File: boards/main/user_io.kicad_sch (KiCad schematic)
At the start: 21 parts, among them J6 FH12-6S-0.5SH(55), J7 FH12-10S-0.5SH(55), P1 JST_BTN_1, P2 JST_BTN_2, P3 JST_BTN_3, U6 BNO085, U7 DRV2605LDGSR

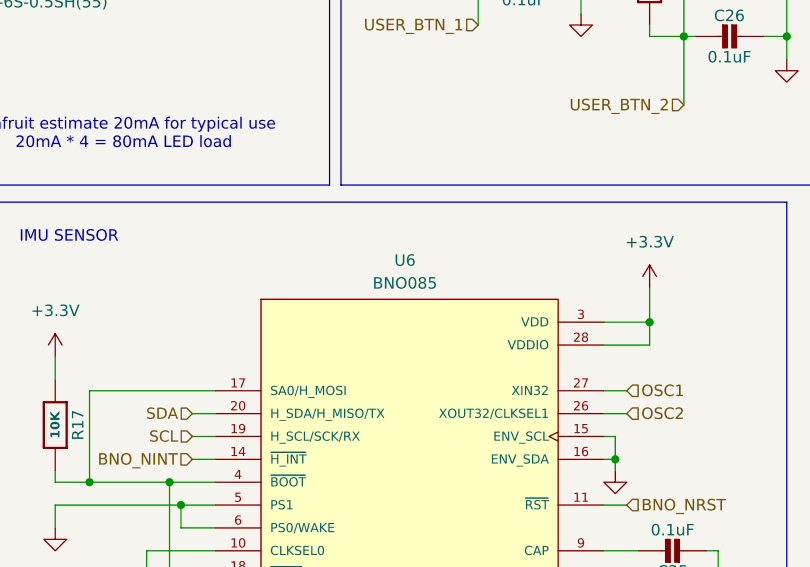
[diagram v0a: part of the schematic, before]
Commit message: Board migrations. Move to newer LED and IMU
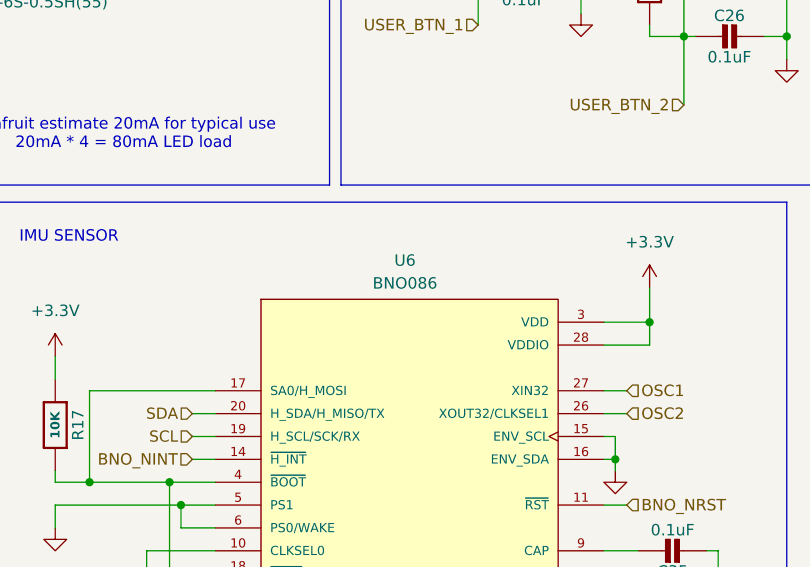
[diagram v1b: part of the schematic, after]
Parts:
- C23, C24, C26, C35: Dielectric (none) -> X7R; DigiKey_PN (none) -> 1276-6844-1-ND; MPN 0402B104K160HI -> CL05B104KO5VPNC; Manufacturer (none) -> Samsung Electro-Mechanics; Voltage (none) -> 16V
- C46, C47: Dielectric (none) -> X7R; DigiKey_PN (none) -> 1276-1184-1-ND; MPN 0603B105K100XD -> CL10B105KA8NNNC; Manufacturer (none) -> Samsung Electro-Mechanics; Voltage (none) -> 25V
- D2: DigiKey_PN (none) -> BAV199LT1GOSCT-ND; MPN BAV199 -> BAV199LT1G; Manufacturer (none) -> onsemi; Sourcing_Note (none) -> OVERSTRESSED AS DRAWN. Pin 3 is the common K1/A2 node, so o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
- HAPTIC1, P1, P2, P3: DigiKey_PN (none) -> 455-1564-1-ND; Manufacturer (none) -> JST Sales America Inc.
- J6: DigiKey_PN (none) -> HFJ106CT-ND; MPN (none) -> FH12-6S-0.5SH(55); Manufacturer (none) -> Hirose Electric Co Ltd; Sourcing_Note (none) -> Digi-Key stock 0, 16-week factory lead. Alternatives: stand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
- J7: DigiKey_PN (none) -> HFJ110CT-ND; MPN (none) -> FH12-10S-0.5SH(55); Manufacturer (none) -> Hirose Electric Co Ltd
- R13: DigiKey_PN (none) -> 13-RT0603BRC07500RLCT-ND; Manufacturer (none) -> YAGEO; Sourcing_Note (none) -> 500R is not an E24 value, so this is a 0.1% thin-film part 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; Tolerance (none) -> 0.1%
- R14, R15, R16, R17: DigiKey_PN (none) -> 311-10.0KHRCT-ND; Manufacturer (none) -> YAGEO; Tolerance (none) -> 1%
- U6: value BNO085 -> BNO086; symbol BNO085:BNO085 -> BNO086:BNO086; DigiKey_PN (none) -> 1888-BNO086CT-ND; MANUFACTURER Hillcrest Laboratories, Inc. -> CEVA Technologies, Inc.; MP BNO085 -> BNO086; MPN BNO085 -> BNO086; Manufacturer (none) -> CEVA Technologies, Inc.; PRICE 10.06 -> 11.62; Sourcing_Note (none) -> BNO086 replaces the deprecated BNO085. Same 28-LGA 5.2x3.8x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
- U7: DigiKey_PN (none) -> 296-40032-1-ND; Manufacturer (none) -> Texas Instruments; Sourcing_Note (none) -> Only ~105 pieces in Digi-Key stock with a 16-week factory l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

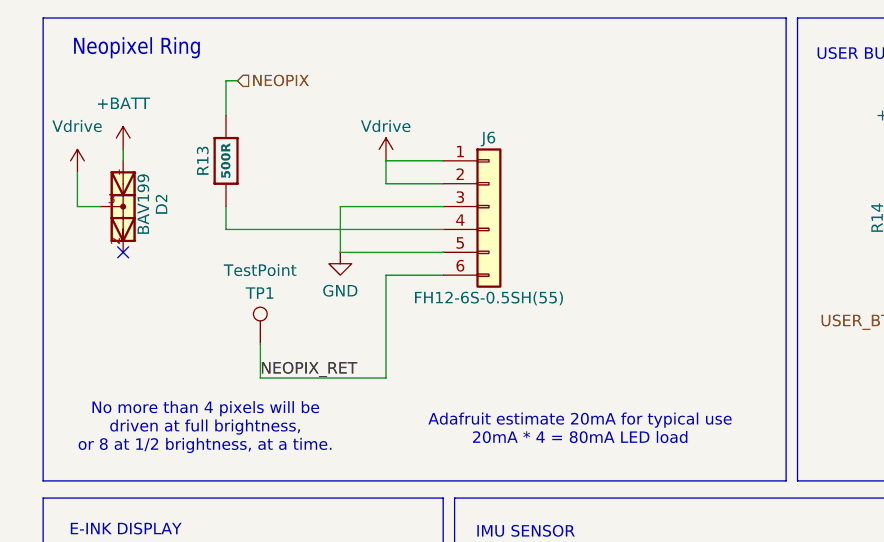
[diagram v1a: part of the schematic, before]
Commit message: some more component reworking. Moved to 10 lane ribbon connects between all boards
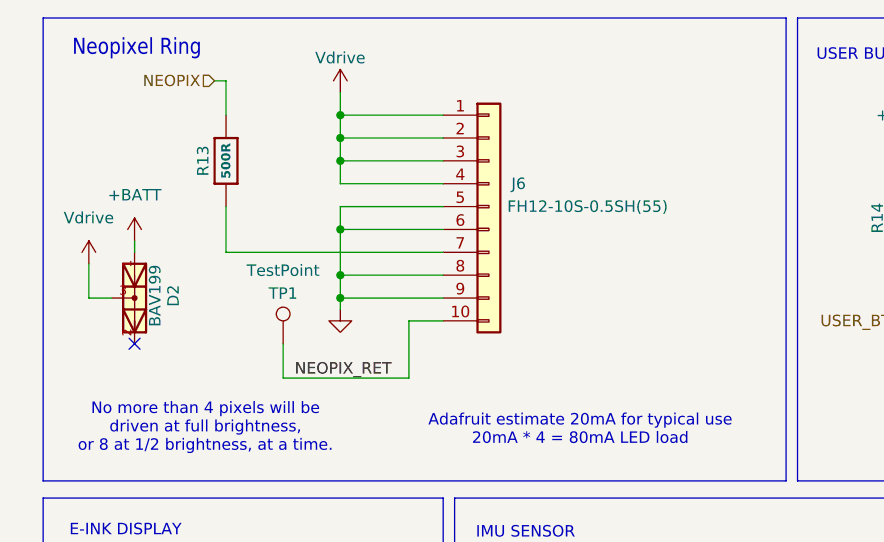
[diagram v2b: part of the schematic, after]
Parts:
- removed J6: FH12-6S-0.5SH(55), Connector_FFC-FPC:Hirose_FH12-6S-0.5SH_1x06-1MP_P0.50mm_Horizontal, symbol Connector_Generic:Conn_01x06
- added J6: FH12-10S-0.5SH(55), Connector_FFC-FPC:Hirose_FH12-10S-0.5SH_1x10-1MP_P0.50mm_Horizontal, symbol Connector_Generic:Conn_01x10
- C23, C24, C26, C35, C46, C47: symbol Adafruit ESP32-S3 8MB No PSRAM-eagle-import:CAP_CERAMIC0603_NO -> smart_compass_main:CAP_CERAMIC0603_NO
- D2: symbol BAV199:BAV199 -> smart_compass_main:BAV199
- HAPTIC1, P1, P2, P3: symbol SM02B-GHS-TB:SM02B-GHS-TB -> smart_compass_main:SM02B-GHS-TB
- R13, R14, R15, R16, R17: symbol Adafruit ESP32-S3 8MB No PSRAM-eagle-import:RESISTOR_0603_NOOUT -> smart_compass_main:RESISTOR_0603_NOOUT
- U6: symbol BNO086:BNO086 -> smart_compass_main:BNO086
- U7: symbol DRV2605LDGSR:DRV2605LDGSR -> smart_compass_main:DRV2605LDGSR
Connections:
- net GND: now also J6.5 (Pin_5), J6.6 (Pin_6), J6.8 (Pin_8), J6.9 (Pin_9)
- net NEOPIX_RET: now also J6.10 (Pin_10)
- net Vdrive: now also J6.1 (Pin_1), J6.2 (Pin_2), J6.3 (Pin_3), J6.4 (Pin_4)
- net at R13.1: now also J6.7 (Pin_7)
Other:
- moved on the sheet: D2, TP1

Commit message: Add a voltage booster and logic shift to the LED ring. Power consumption implications, but necessary
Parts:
- removed D2: BAV199, BAV199:SOT23, symbol smart_compass_main:BAV199
- added C15: 22uF, Capacitor_SMD:C_0805_2012Metric, symbol Device:C
- added FB1: 600R@100MHz, Inductor_SMD:L_0603_1608Metric, symbol Device:FerriteBead
- HAPTIC1, P1, P2, P3: footprint SM02B-GHS-TB:JST_SM02B-GHS-TB -> (none)
- J3: renamed from J6; Sourcing_Note Standardised on the 10-way FH12 shared with the display lin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 -> Vdrive on 1-3, RING_EN on 4, GND on 5, 6, 8, 9, NEOPIX on 7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
- R13: Sourcing_Note 500R is not an E24 value, so this is a 0.1% thin-film part at $0.25. For a series damping resistor a 5% 510R (RC0603JR-07511RL) would do the same job for about $0.01. -> 500R is not an E24 value, so this is a 0.1% thin-film part at $0.25. For a series damping resistor a 5% 510R (RC0603JR-07511RL) would do the same job for about $0.01. It has a second job now the ring runs at 5V: when RING_EN is low the ring board's level shifter is unpowered, and this resistor limits the current into its input clamp if firmware drives NEOPIX high while the ring is off.
- U6: footprint BNO085:IC_BNO085 -> (none)
- U7: footprint DRV2605LDGSR:SOP50P490X110-10N -> (none)
- renumbered C23 to C16, C24 to C17, C26 to C18, C35 to C19, C46 to C20, C47 to C21, J7 to J4
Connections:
- net +BATT: now also FB1.1
- net GND: now also C15.2
- net Vdrive: now also C15.1, FB1.2; no longer J3.4 (Pin_4)
- new net RING_EN: J3.4 (Pin_4)
- no-connect marks 1 -> 0
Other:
- note removed: "No more than 4 pixels will be driven at full brightness, or 8 at 1/2 brightness, at a time."

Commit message: Update the footprint for the flash chip
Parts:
- renumbered C15 to C14, C16 to C15, C17 to C16, C18 to C17, C19 to C18, C20 to C19, C21 to C20

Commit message: UPGRADE 1UF CAPACITORS
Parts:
- C19, C20: DigiKey_PN 1276-1184-1-ND -> 445-C1608X7R1H105K080ABCT-ND; MPN CL10B105KA8NNNC -> C1608X7R1H105K080AB; Manufacturer Samsung Electro-Mechanics -> TDK; PRICE 0.05765 -> 0.0615; Tolerance (none) -> 10%; Voltage 25V -> 50V
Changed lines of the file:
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@@
 			)
 		)
-		(property "Datasheet" ""
+		(property "Datasheet" "https://product.tdk.com/system/files/dam/doc/product/capacitor/ceramic/mlcc/catalog/mlcc_commercial_general_en.pdf"
 			(at 83.82 163.83 0)
 			(hide yes)
@@
 			)
 		)
-		(property "MPN" "CL10B105KA8NNNC"
+		(property "MPN" "C1608X7R1H105K080AB"
 			(at 83.82 163.83 90)
 			(hide yes)
@@
 			)
 		)
-		(property "PRICE" "0.05765"
+		(property "PRICE" "0.0615"
 			(at 83.82 163.83 90)
 			(hide yes)
@@
 			)
 		)
-		(property "Manufacturer" "Samsung Electro-Mechanics"
+		(property "Manufacturer" "TDK"
 			(at 83.82 163.83 0)
 			(hide yes)
@@
 			)
 		)
-		(property "DigiKey_PN" "1276-1184-1-ND"
+		(property "DigiKey_PN" "445-C1608X7R1H105K080ABCT-ND"
 			(at 83.82 163.83 0)
 			(hide yes)
@@
 			)
 		)
-		(property "Voltage" "25V"
+		(property "Voltage" "50V"
 			(at 83.82 163.83 0)
 			(hide yes)
@@
 			)
 		)
+    (property "Tolerance" "10%" (at 83.82 163.83 0)
+      (effects (font (size 1.27 1.27)) (hide yes))
+    )
 		(pin "1"
 		)
@@
 			)
 		)
-		(property "Datasheet" ""
+		(property "Datasheet" "https://product.tdk.com/system/files/dam/doc/product/capacitor/ceramic/mlcc/catalog/mlcc_commercial_general_en.pdf"
 			(at 20.32 148.59 0)
 			(hide yes)
@@
 			)
 		)
-		(property "MPN" "CL10B105KA8NNNC"
+		(property "MPN" "C1608X7R1H105K080AB"
 			(at 20.32 148.59 90)
 			(hide yes)
@@
 			)
 		)
-		(property "PRICE" "0.05765"
+		(property "PRICE" "0.0615"
 			(at 20.32 148.59 90)
 			(hide yes)
@@
 			)
 		)
-		(property "Manufacturer" "Samsung Electro-Mechanics"
+		(property "Manufacturer" "TDK"
 			(at 20.32 148.59 0)
 			(hide yes)
@@
 			)
 		)
-		(property "DigiKey_PN" "1276-1184-1-ND"
+		(property "DigiKey_PN" "445-C1608X7R1H105K080ABCT-ND"
 			(at 20.32 148.59 0)
 			(hide yes)
@@
 			)
 		)
-		(property "Voltage" "25V"
+		(property "Voltage" "50V"
 			(at 20.32 148.59 0)
 			(hide yes)
@@
 			)
 		)
+    (property "Tolerance" "10%" (at 20.32 148.59 0)
+      (effects (font (size 1.27 1.27)) (hide yes))
+    )
 		(pin "1"
 		)

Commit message: Ditch the JST for the buttons, power switch, and haptic motor. Just solder direct
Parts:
- removed HAPTIC1: JST_HAPTIC, symbol smart_compass_main:SM02B-GHS-TB
- removed P1: JST_BTN_1, symbol smart_compass_main:SM02B-GHS-TB
- removed P2: JST_BTN_2, symbol smart_compass_main:SM02B-GHS-TB
- removed P3: JST_BTN_3, symbol smart_compass_main:SM02B-GHS-TB
- added HAPTIC1: HAPTIC_PADS, Connector_Wire:SolderWire-0.127sqmm_1x02_P3.7mm_D0.48mm_OD1mm_Relief, symbol Connector_Generic:Conn_01x02
- added P1: BUTTON_PADS, Connector_Wire:SolderWire-0.127sqmm_1x04_P3.7mm_D0.48mm_OD1mm_Relief, symbol Connector_Generic:Conn_01x04
- renumbered C16 to C15, C17 to C16, C15 to C17, R15 to R14, R16 to R15, R14 to R16
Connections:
- net GND: now also P1.4 (Pin_4)
- net USER_BTN_1: now also P1.1 (Pin_1)
- net USER_BTN_2: now also P1.2 (Pin_2)
- net USER_BTN_3: now also P1.3 (Pin_3)
- net at U7.7 (OUT+): now also HAPTIC1.1 (Pin_1)
- net at U7.9 (OUT-): now also HAPTIC1.2 (Pin_2)
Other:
- note added: "Bond the splice down; it sits on a moving mass."
- note added: "Pigtail to the LRA, soldered straight to the board. Thin UL3302 32/34 AWG to the actuator pads, spliced within ~10mm to 28 AWG, and that run solders into these pads."
- note removed: "This will connect to a pigtail for the LRA. I intend to hand-solder thin wires to the actuator, then join those to slightly thicker wires which are crimped to the JST connector"
- moved on the sheet: C15, C16, C17, R14, R15, R16

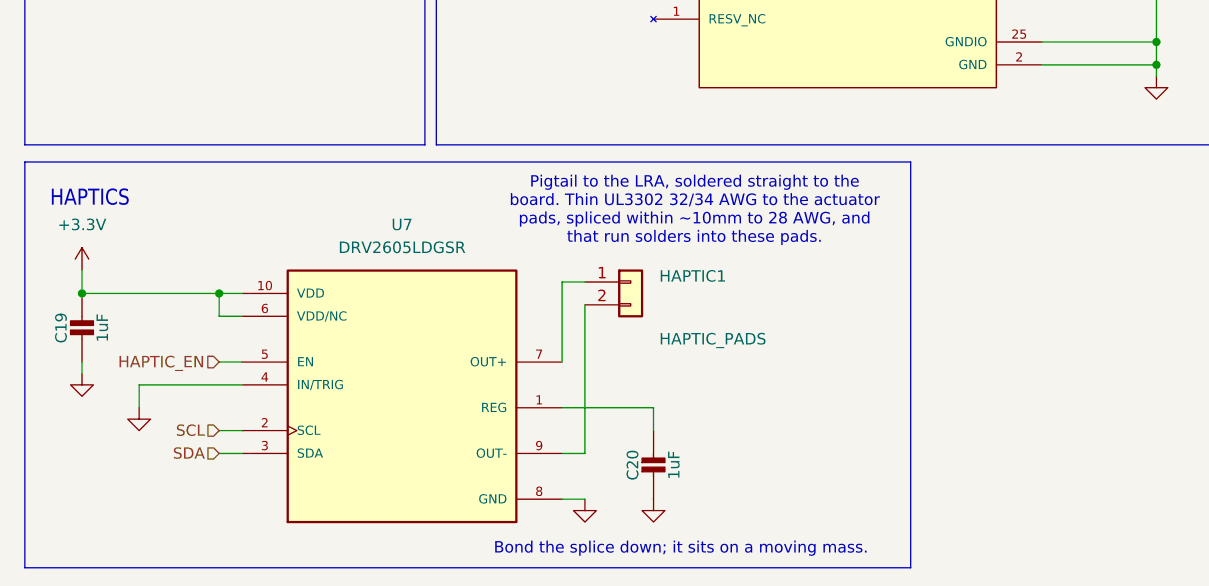
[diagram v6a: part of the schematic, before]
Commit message: DMG3415U was superceeded - swap it out and update the docs. Also add another bulk cap to the haptic driver to accommodate the new motor
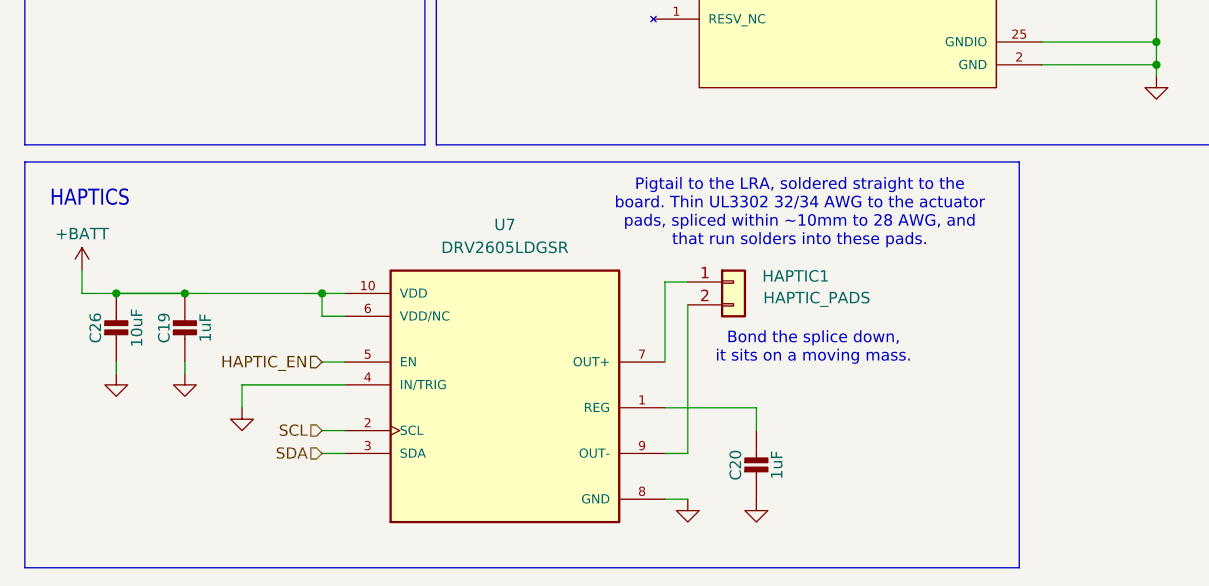
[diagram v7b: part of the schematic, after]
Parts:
- added C26: 10uF, Capacitor_SMD:C_0805_2012Metric, symbol smart_compass_main:CAP_CERAMIC0805-NOOUTLINE
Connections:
- net +3.3V: no longer C19.1, U7.10 (VDD), U7.6 (VDD/NC)
- net +BATT: now also C19.1, U7.10 (VDD), U7.6 (VDD/NC), C26.1
- net GND: now also C26.2
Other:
- note added: "Bond the splice down, it sits on a moving mass."
- note removed: "Bond the splice down; it sits on a moving mass."
- moved on the sheet: C19, C20, HAPTIC1, U7

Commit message: grab a bunch of datasheets. Fix some models, fix some footprints, replace an unsuited capacitor
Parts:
- HAPTIC1: DigiKey_PN 455-1564-1-ND -> (none); DigiKey_Part_Number 455-1564-1-ND -> (none); MANUFACTURER JST -> (none); MF JST Sales -> (none); MP SM02B-GHS-TB -> (none); MPN SM02B-GHS-TB -> (none); Manufacturer JST Sales America Inc. -> (none); PRICE 0.26 -> (none)
- U6: MANUFACTURER CEVA Technologies, Inc. -> (none)
- U7: MANUFACTURER Texas Instruments -> (none)
- renumbered C26 to C19, C19 to C20, C20 to C21
